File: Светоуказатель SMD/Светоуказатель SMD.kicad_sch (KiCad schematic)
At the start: 64 parts, among them J1 DB-9 RS232, J2 Отладка SWD, Q1 S8550, Q2 S8550, SW1 SW_Push, U1 TPS5430DDA, U2 AMS1117-3.3, U3 STM32F103C8Tx, U4 MAX3232, U5 ADuM1201AR, Y1 8 МГц

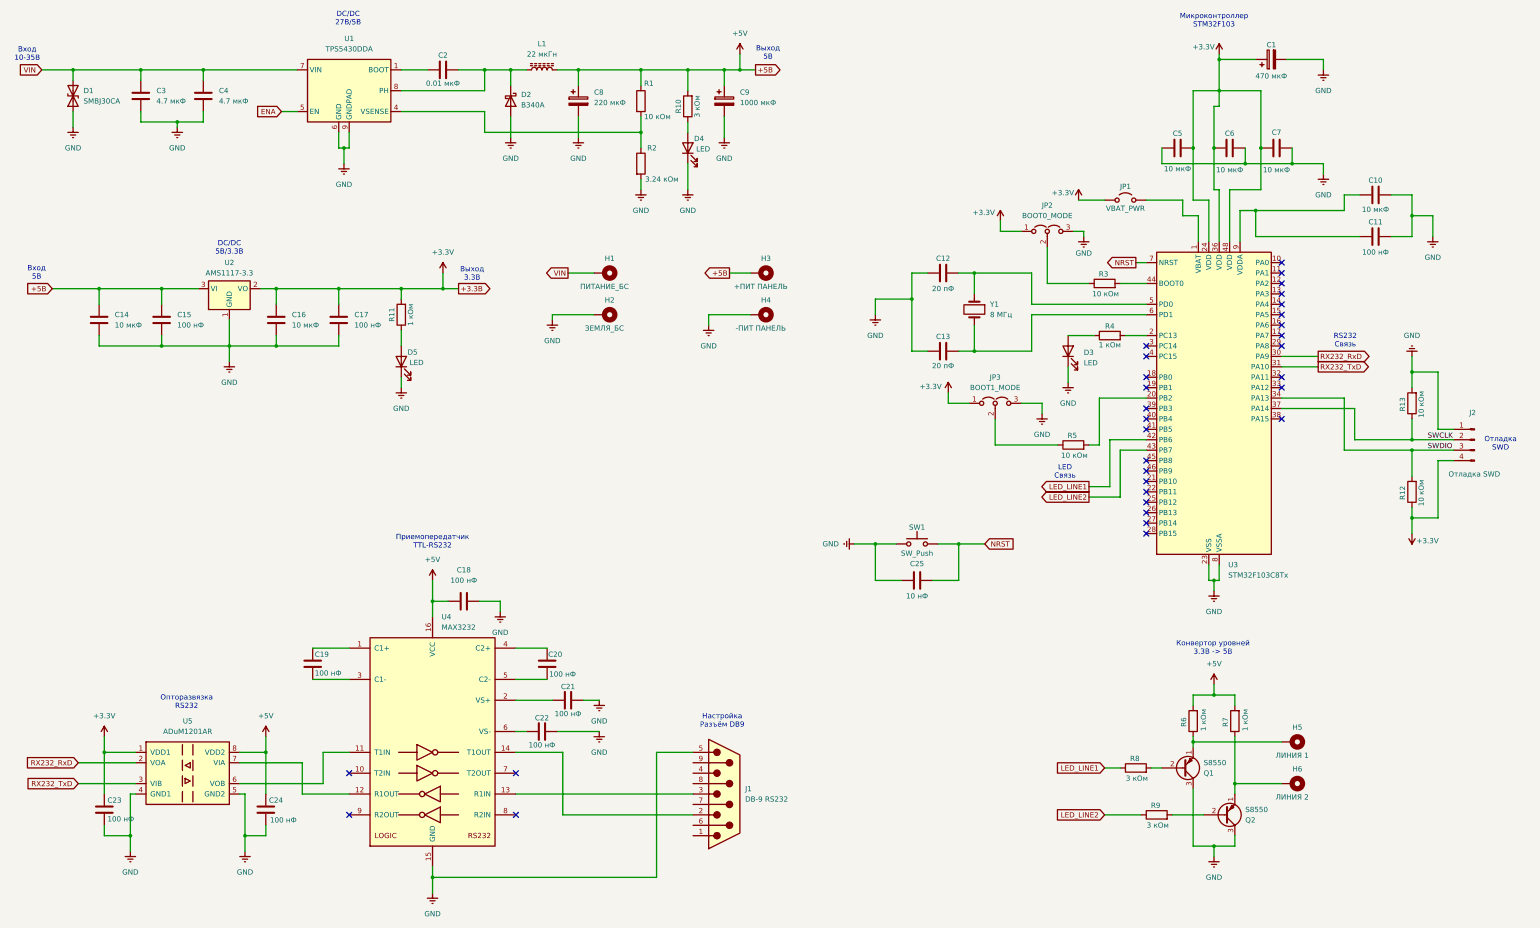
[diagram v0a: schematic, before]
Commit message: Add PCB file.
Add pcb and components to project.
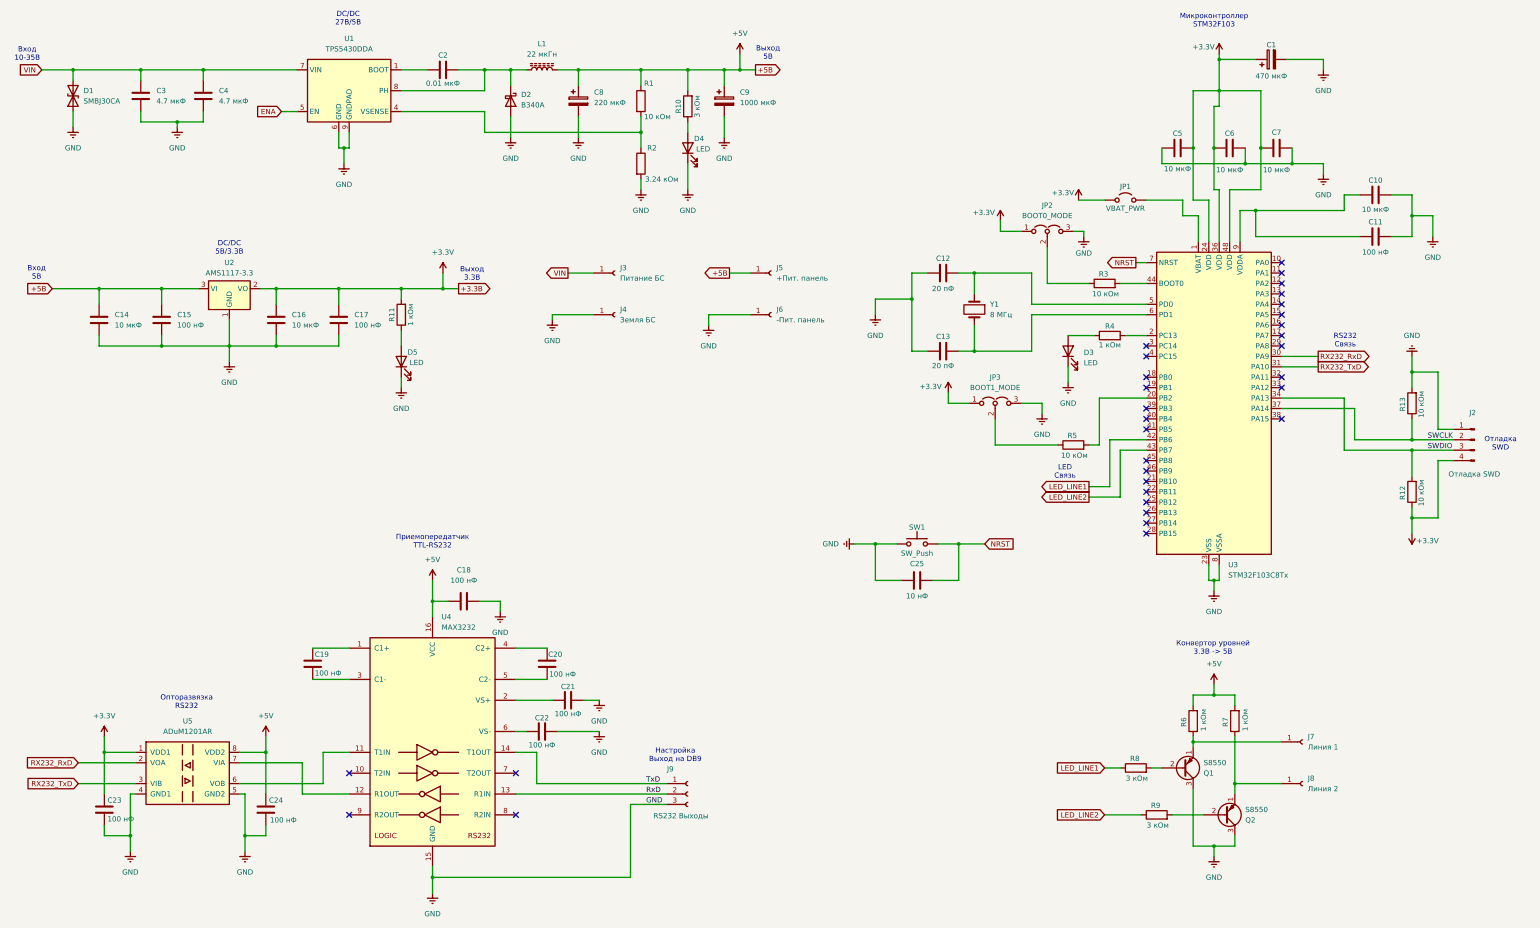
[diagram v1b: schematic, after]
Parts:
- removed H1: ПИТАНИЕ_БС, MountingHole:MountingHole_2.5mm_Pad_Via, symbol Mechanical:MountingHole_Pad_MP
- removed H2: ЗЕМЛЯ_БС, MountingHole:MountingHole_2.5mm_Pad_Via, symbol Mechanical:MountingHole_Pad_MP
- removed H3: +ПИТ ПАНЕЛЬ, MountingHole:MountingHole_2.5mm_Pad_Via, symbol Mechanical:MountingHole_Pad_MP
- removed H4: -ПИТ ПАНЕЛЬ, MountingHole:MountingHole_2.5mm_Pad_Via, symbol Mechanical:MountingHole_Pad_MP
- removed H5: ЛИНИЯ 1, MountingHole:MountingHole_2.5mm_Pad_Via, symbol Mechanical:MountingHole_Pad_MP
- removed H6: ЛИНИЯ 2, MountingHole:MountingHole_2.5mm_Pad_Via, symbol Mechanical:MountingHole_Pad_MP
- removed J1: DB-9 RS232, Connector_Dsub:DSUB-9_Male_Vertical_P2.77x2.84mm, symbol Connector:DE9_Plug
- added J3: Питание БС, Connector_Wire:SolderWire-2.5sqmm_1x01_D2.4mm_OD4.4mm, symbol Connector:Conn_01x01_Socket
- added J4: Земля БС, Connector_Wire:SolderWire-2.5sqmm_1x01_D2.4mm_OD4.4mm, symbol Connector:Conn_01x01_Socket
- added J5: +Пит. панель, Connector_Wire:SolderWire-2.5sqmm_1x01_D2.4mm_OD4.4mm, symbol Connector:Conn_01x01_Socket
- added J6: -Пит. панель, Connector_Wire:SolderWire-2.5sqmm_1x01_D2.4mm_OD4.4mm, symbol Connector:Conn_01x01_Socket
- added J7: Линия 1, Connector_Wire:SolderWire-2.5sqmm_1x01_D2.4mm_OD4.4mm, symbol Connector:Conn_01x01_Socket
- added J8: Линия 2, Connector_Wire:SolderWire-2.5sqmm_1x01_D2.4mm_OD4.4mm, symbol Connector:Conn_01x01_Socket
- added J9: RS232 Выходы, Connector_Wire:SolderWire-1sqmm_1x03_P7.8mm_D1.4mm_OD3.9mm, symbol Connector:Conn_01x03_Socket
- Q1, Q2: footprint Package_TO_SOT_THT:TO-92_Inline -> Package_TO_SOT_SMD:SOT-23
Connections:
- net +5V: now also J5.1 (Pin_1)
- net GND: now also J4.1 (Pin_1), J6.1 (Pin_1), J9.3 (Pin_3)
- net VIN: now also J3.1 (Pin_1)
- net at Q2.1 (E), R7.1: now also J8.1 (Pin_1)
- net at Q1.1 (E), R6.1: now also J7.1 (Pin_1)
- net RxD: now reaches U4.13 (R1IN)
- net RxD: now also J9.2 (Pin_2)
- net TxD: now reaches U4.14 (T1OUT)
- net TxD: now also J9.1 (Pin_1)
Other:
- note added: "Настройка Выход на DB9"
- note removed: "Настройка Разъём DB9"

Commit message: Add full component places.
Set component places for board without routing.
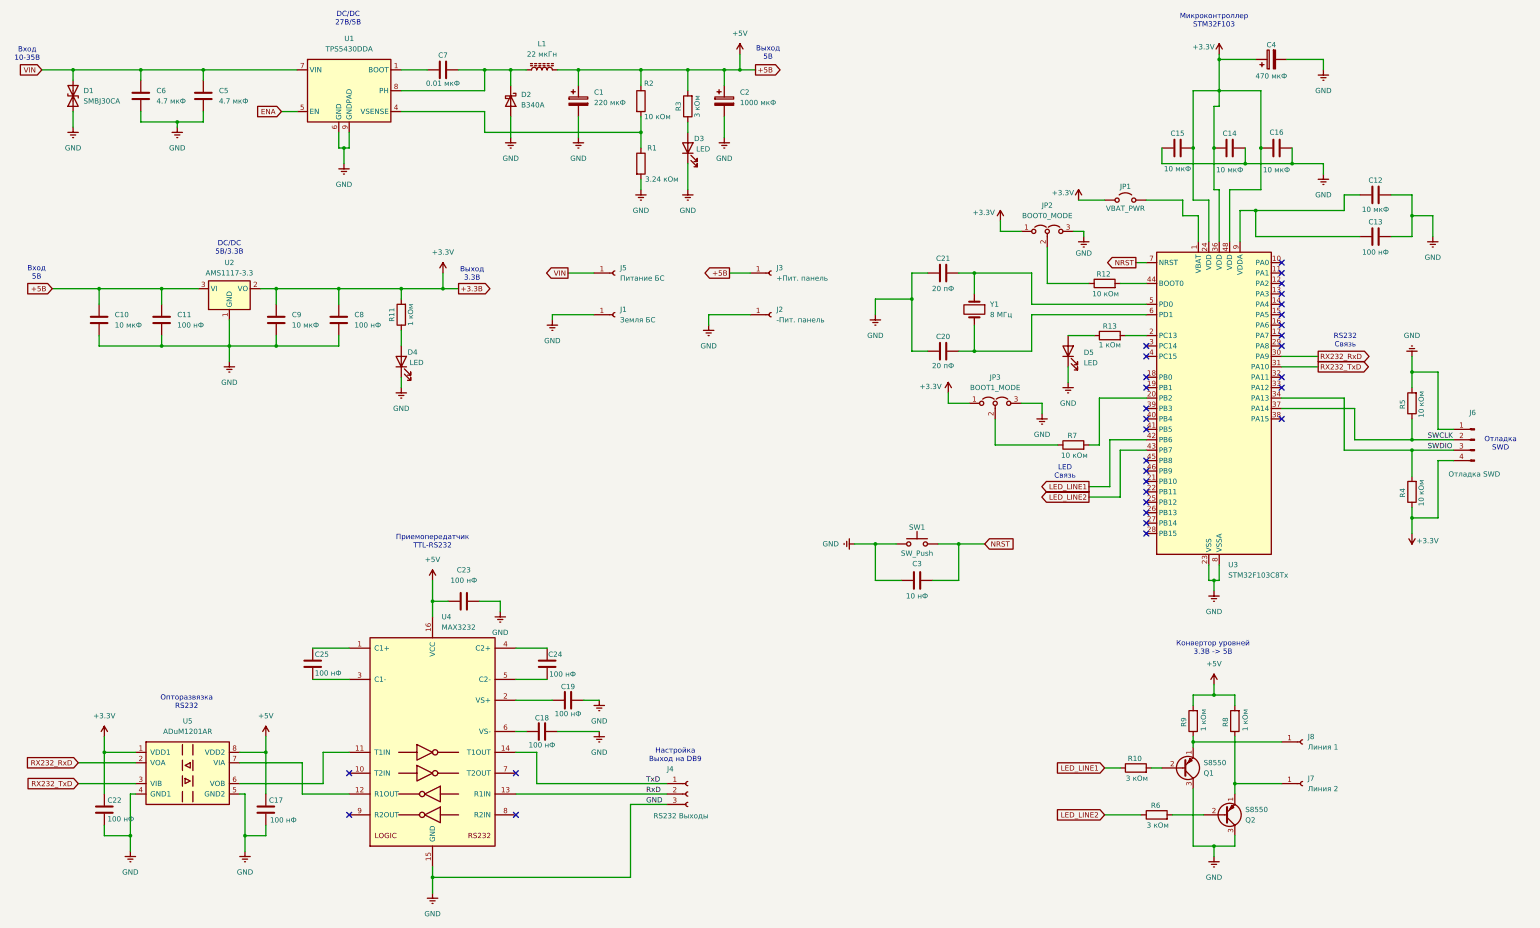
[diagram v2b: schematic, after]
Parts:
- renumbered C8 to C1, C14 to C10, C15 to C11, C10 to C12, C11 to C13, C6 to C14, C5 to C15, C7 to C16, C24 to C17, C22 to C18, C21 to C19, C9 to C2, C13 to C20, C12 to C21, C23 to C22, C18 to C23, C20 to C24, C19 to C25, C25 to C3, C1 to C4, C4 to C5, C3 to C6, C2 to C7, C17 to C8, C16 to C9, D4 to D3, D5 to D4, D3 to D5, J4 to J1, J6 to J2, J5 to J3, J9 to J4, J3 to J5, J2 to J6, J8 to J7, J7 to J8, R2 to R1, R8 to R10, R3 to R12, R4 to R13, R1 to R2, R10 to R3, R12 to R4, R13 to R5, R9 to R6, R5 to R7, R7 to R8, R6 to R9

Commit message: Full routing add.
Complete full touting for board.
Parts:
- removed JP1: VBAT_PWR, Connector_PinHeader_2.54mm:PinHeader_1x02_P2.54mm_Vertical, symbol Jumper:Jumper_2_Open
- removed JP2: BOOT0_MODE, Connector_PinHeader_2.54mm:PinHeader_1x03_P2.54mm_Vertical, symbol Jumper:Jumper_3_Open
- removed JP3: BOOT1_MODE, Connector_PinHeader_2.54mm:PinHeader_1x03_P2.54mm_Vertical, symbol Jumper:Jumper_3_Open
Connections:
- net +3.3V: now also R12.1, R7.1
- no-connect marks 31 -> 32

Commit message: Cap moved.
Move cap from electro to tantal.
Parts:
- C2, C4: footprint Capacitor_SMD:CP_Elec_10x10.5 -> Capacitor_Tantalum_SMD:CP_EIA-7343-43_Kemet-X_Pad2.25x2.55mm_HandSolder
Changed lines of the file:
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@@
 			)
 		)
-		(property "Footprint" "Capacitor_SMD:CP_Elec_10x10.5"
+		(property "Footprint" "Capacitor_Tantalum_SMD:CP_EIA-7343-43_Kemet-X_Pad2.25x2.55mm_HandSolder"
 			(at 205.4352 54.61 0)
 			(effects
@@
 			)
 		)
-		(property "Footprint" "Capacitor_SMD:CP_Elec_10x10.5"
+		(property "Footprint" "Capacitor_Tantalum_SMD:CP_EIA-7343-43_Kemet-X_Pad2.25x2.55mm_HandSolder"
 			(at 341.63 39.6748 0)
 			(effects
